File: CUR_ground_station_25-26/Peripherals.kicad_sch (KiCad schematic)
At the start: 18 parts, among them Q1 NTR4003N, SW1 PTS815SJM250SMTRLFS, SW2 PTS815SJM250SMTRLFS, SW3 PTS815SJM250SMTRLFS, SW4 PTS815SJM250SMTRLFS, U6 2.13" Epaper Module

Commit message: started layout-ing
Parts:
- BZ1: footprint Buzzer_SameSky:XDCR_CMT-7525-03-SMT-TR -> Buzzer_SameSky:Buzzer_SameSky_CEM-1203_42
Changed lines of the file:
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@@
 			)
 		)
-		(property "Footprint" "Buzzer_SameSky:XDCR_CMT-7525-03-SMT-TR"
+		(property "Footprint" "Buzzer_SameSky:Buzzer_SameSky_CEM-1203_42"
 			(at 255.905 27.94 90)
 			(effects

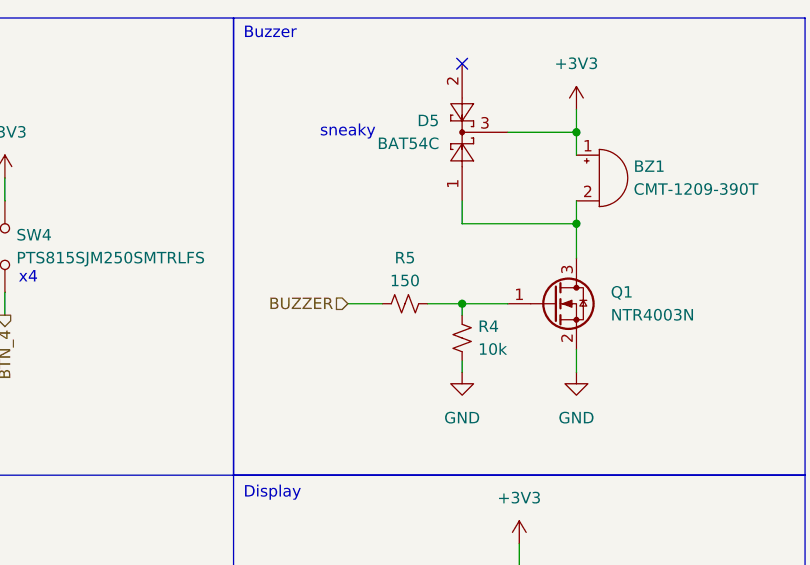
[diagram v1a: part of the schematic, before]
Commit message: BOM optimization
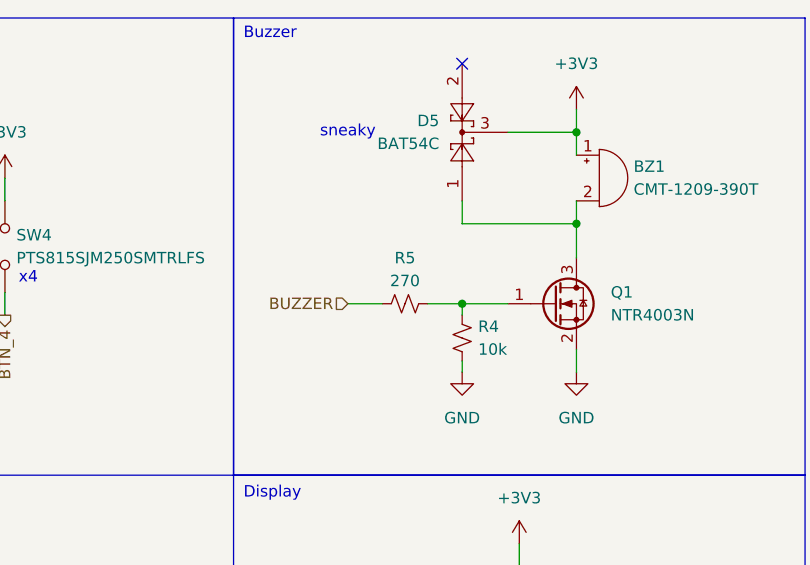
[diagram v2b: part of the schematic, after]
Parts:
- R5: value 150 -> 270
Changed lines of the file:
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@@
 			)
 		)
-		(property "Value" "150"
+		(property "Value" "270"
 			(at 234.95 41.91 90)
 			(effects

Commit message: switched battery connector, put mounting holes in place
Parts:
- BZ1: footprint Buzzer_SameSky:Buzzer_SameSky_CEM-1203_42 -> Buzzer_SameSky:Buzzer_SameSky_CPT-1207-3TH
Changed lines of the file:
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@@
 			)
 		)
-		(property "Footprint" "Buzzer_SameSky:Buzzer_SameSky_CEM-1203_42"
+		(property "Footprint" "Buzzer_SameSky:Buzzer_SameSky_CPT-1207-3TH"
 			(at 255.905 27.94 90)
 			(effects

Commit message: preliminary 3v3 rail routed
routed on top layer. Its...interesting...
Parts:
- BZ1: footprint Buzzer_SameSky:Buzzer_SameSky_CPT-1207-3TH -> Buzzer_SameSky:XDCR_CMT-7525-03-SMT-TR
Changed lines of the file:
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@@
 			)
 		)
-		(property "Footprint" "Buzzer_SameSky:Buzzer_SameSky_CPT-1207-3TH"
+		(property "Footprint" "Buzzer_SameSky:XDCR_CMT-7525-03-SMT-TR"
 			(at 255.905 27.94 90)
 			(effects

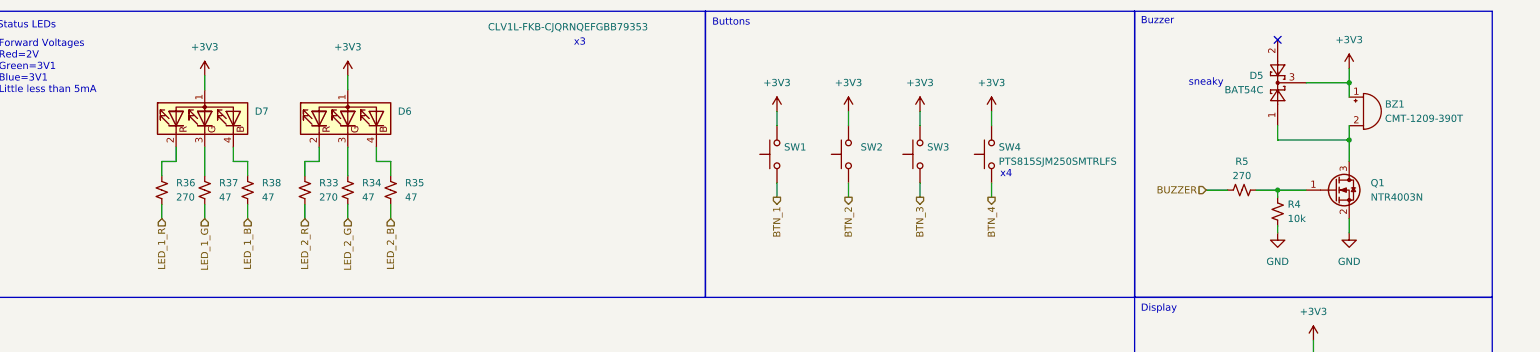
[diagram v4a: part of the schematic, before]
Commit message: Find MPNs again
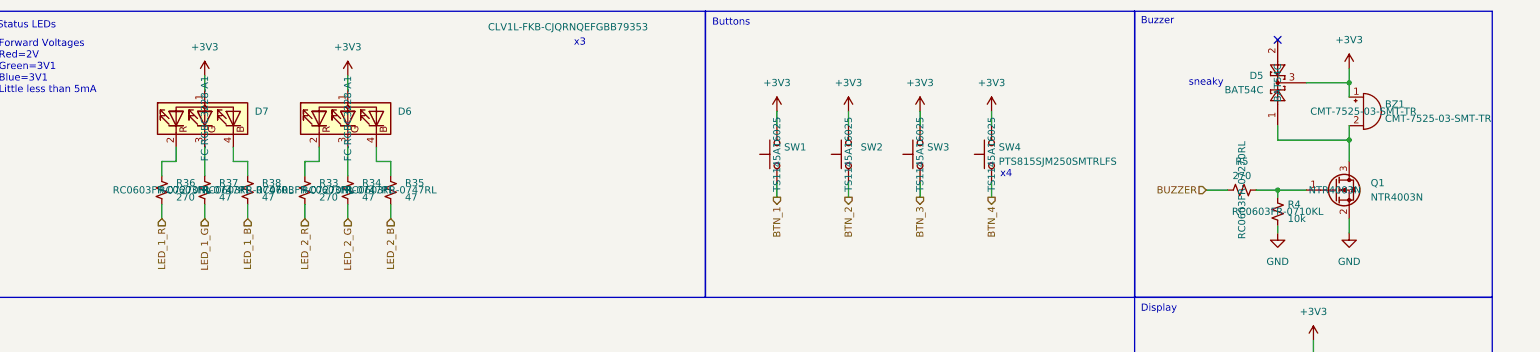
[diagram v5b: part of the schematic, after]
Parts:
- BZ1: value CMT-1209-390T -> CMT-7525-03-SMT-TR; MPN (none) -> CMT-7525-03-SMT-TR
- D5: MPN (none) -> BAT54C
- D6, D7: MPN (none) -> FC-RGBC3228-A1
- Q1: MPN (none) -> NTR4003N; now left out of the parts list
- R33, R36, R5: MPN (none) -> RC0603FR-07270RL
- R34, R35, R37, R38: MPN (none) -> RC0603FR-0747RL
- R4: MPN (none) -> RC0603FR-0710KL
- SW1, SW2, SW3, SW4: MPN (none) -> TS1145A16025
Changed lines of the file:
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@@
+			)
+		)
+		(property "MPN" "TS1145A16025"
+			(at 165.1 38.1 0)
+			(effects
+				(font
+					(size 1.27 1.27)
+				)
 			)
 		)
@@
 			)
 		)
+		(property "MPN" "FC-RGBC3228-A1"
+			(at 50.8 31.75 0)
+			(effects
+				(font
+					(size 1.27 1.27)
+				)
+			)
+		)
 		(pin "2"
 		)
@@
 			)
 		)
+		(property "MPN" "RC0603FR-07270RL"
+			(at 234.95 44.45 0)
+			(effects
+				(font
+					(size 1.27 1.27)
+				)
+			)
+		)
 		(pin "1"
 		)
@@
 			)
 		)
+		(property "MPN" " RC0603FR-0747RL"
+			(at 76.2 44.45 0)
+			(effects
+				(font
+					(size 1.27 1.27)
+				)
+			)
+		)
 		(pin "2"
 		)
@@
 			)
 		)
+		(property "MPN" " RC0603FR-0747RL"
+			(at 58.42 44.45 0)
+			(effects
+				(font
+					(size 1.27 1.27)
+				)
+			)
+		)
 		(pin "2"
 		)
@@
 		(unit 1)
 		(exclude_from_sim no)
-		(in_bom yes)
+		(in_bom no)
 		(on_board yes)
 		(dnp no)
@@
 			)
 		)
+		(property "MPN" "NTR4003N"
+			(at 251.46 44.45 0)
+			(effects
+				(font
+					(size 1.27 1.27)
+				)
+			)
+		)
 		(pin "1"
 		)
@@
 			)
 		)
+		(property "MPN" " RC0603FR-0747RL"
+			(at 50.8 44.45 0)
+			(effects
+				(font
+					(size 1.27 1.27)
+				)
+			)
+		)
 		(pin "2"
 		)
@@
 			)
 		)
+		(property "MPN" "BAT54C"
+			(at 241.3 25.4 0)
+			(effects
+				(font
+					(size 1.27 1.27)
+				)
+			)
+		)
 		(pin "3"
 		)
@@
 			)
 		)
-		(property "Value" "CMT-1209-390T"
+		(property "Value" "CMT-7525-03-SMT-TR"
 			(at 260.35 31.7499 0)
 			(effects
@@
 			)
 		)
+		(property "MPN" "CMT-7525-03-SMT-TR"
+			(at 256.54 30.48 0)
+			(effects
+				(font
+					(size 1.27 1.27)
+				)
+			)
+		)
 		(pin "2"
 		)
@@
 			)
 		)
+		(property "MPN" "TS1145A16025"
+			(at 190.5 38.1 0)
+			(effects
+				(font
+					(size 1.27 1.27)
+				)
+			)
+		)
 		(pin "2"
 		)
@@
 			)
 		)
+		(property "MPN" "TS1145A16025"
+			(at 152.4 38.1 0)
+			(effects
+				(font
+					(size 1.27 1.27)
+				)
+			)
+		)
 		(pin "2"
 		)
@@
 			)
 		)
+		(property "MPN" " RC0603FR-0747RL"
+			(at 83.82 44.45 0)
+			(effects
+				(font
+					(size 1.27 1.27)
+				)
+			)
+		)
 		(pin "2"
 		)
@@
 			)
 		)
+		(property "MPN" "RC0603FR-07270RL"
+			(at 43.18 44.45 0)
+			(effects
+				(font
+					(size 1.27 1.27)
+				)
+			)
+		)
 		(pin "2"
 		)
@@
 			)
 		)
+		(property "MPN" "RC0603FR-0710KL"
+			(at 241.3 48.26 0)
+			(effects
+				(font
+					(size 1.27 1.27)
+				)
+			)
+		)
 		(pin "1"
 		)
@@
 			)
 		)
+		(property "MPN" "TS1145A16025"
+			(at 177.8 38.1 0)
+			(effects
+				(font
+					(size 1.27 1.27)
+				)
+			)
+		)
 		(pin "2"
 		)
@@
 			)
 		)
+		(property "MPN" "FC-RGBC3228-A1"
+			(at 76.2 31.75 0)
+			(effects
+				(font
+					(size 1.27 1.27)
+				)
+			)
+		)
 		(pin "2"
 		)
@@
 			)
 		)
+		(property "MPN" "RC0603FR-07270RL"
+			(at 68.58 44.45 0)
+			(effects
+				(font
+					(size 1.27 1.27)
+				)
+			)
+		)

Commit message: changes
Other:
- company: (none) -> Clarkson University Rocketry
- title: (none) -> Ground Station
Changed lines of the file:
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@@
 	(generator_version "9.0")
 	(paper "A4")
+	(title_block
+		(title "Ground Station")
+		(date "2026-04-29")
+		(company "Clarkson University Rocketry")
+	)
 	(rectangle
 		(start 215.9 12.7)
@@
 					(size 1.27 1.27)
 				)
+				(hide yes)
 			)
 		)
@@
 					(size 1.27 1.27)
 				)
+				(hide yes)
 			)
 		)
@@
 					(size 1.27 1.27)
 				)
+				(hide yes)
 			)
 		)
@@
 					(size 1.27 1.27)
 				)
+				(hide yes)
 			)
 		)
@@
 					(size 1.27 1.27)
 				)
+				(hide yes)
 			)
 		)
@@
 					(size 1.27 1.27)
 				)
+				(hide yes)
 			)
 		)
@@
 					(size 1.27 1.27)
 				)
+				(hide yes)
 			)
 		)
@@
 					(size 1.27 1.27)
 				)
+				(hide yes)
 			)
 		)
@@
 					(size 1.27 1.27)
 				)
+				(hide yes)
 			)
 		)
@@
 					(size 1.27 1.27)
 				)
+				(hide yes)
 			)
 		)
@@
 					(size 1.27 1.27)
 				)
+				(hide yes)
 			)
 		)
@@
 					(size 1.27 1.27)
 				)
+				(hide yes)
 			)
 		)
@@
 					(size 1.27 1.27)
 				)
+				(hide yes)
 			)
 		)
@@
 					(size 1.27 1.27)
 				)
+				(hide yes)
 			)
 		)
@@
 					(size 1.27 1.27)
 				)
+				(hide yes)
 			)
 		)
@@
 					(size 1.27 1.27)
 				)
+				(hide yes)
 			)
 		)
@@
 					(size 1.27 1.27)
 				)
+				(hide yes)
 			)
 		)
@@
 					(unit 1)
 				)
+			)
+		)
+	)
+	(symbol
+		(lib_id "CUR_Logo:LOGO")
+		(at 279.4 173.99 0)
+		(unit 1)
+		(exclude_from_sim no)
+		(in_bom yes)
+		(on_board yes)
+		(dnp no)
+		(fields_autoplaced yes)
+		(property "Reference" "#G5"
+			(at 279.4 167.002 0)
+			(effects
+				(font
+					(size 1.27 1.27)
+				)
+				(hide yes)
+			)
+		)
+		(property "Value" "LOGO"
+			(at 279.4 180.978 0)
+			(effects
+				(font
+					(size 1.27 1.27)
+				)
+				(hide yes)
+			)
+		)
+		(property "Footprint" ""
+			(at 279.4 173.99 0)
+			(effects
+				(font
+					(size 1.27 1.27)
+				)
+				(hide yes)
+			)
+		)
+		(property "Datasheet" ""
+			(at 279.4 173.99 0)
+			(effects
+				(font
+					(size 1.27 1.27)
+				)
+				(hide yes)
+			)
+		)
+		(property "Description" ""
+			(at 279.4 173.99 0)
+			(effects
+				(font
+					(size 1.27 1.27)
+				)
+				(hide yes)
+			)
+		)
+		(instances
+			(project "CUR_ground_station_25-26"
+				(path "/b6f682bd-f29b-4650-adb4-b230be0368ad/2d813cf0-bc84-4162-82ae-548df427bc37"
+					(reference "#G5")
+					(unit 1)
+				)
